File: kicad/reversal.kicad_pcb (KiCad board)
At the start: 2 copper layers, 256.2 x 134.5 mm, 27 parts, among them J1 USB_A

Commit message: reduced left edge of pcb
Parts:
- moved H4 19.9 mm to (256.0, 153.0)
- moved H3 15.3 mm to (29.0, 153.0)
- moved H5 4.84 mm to (29.0, 42.7)
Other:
- board size 256.2 x 134.5 mm -> 251.2 x 134.5 mm
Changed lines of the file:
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@@
   (net 27 "unconnected-(A1-3V3-Pad21)")
   (footprint "MountingHole:MountingHole_6.4mm_M6" (layer "F.Cu")
-    (at 24.16 42.7)
+    (at 29 42.7)
     (descr "Mounting Hole 6.4mm, no annular, M6")
     (tags "mounting hole 6.4mm no annular m6")
@@
   )
   (footprint "MountingHole:MountingHole_6.4mm_M6" (layer "F.Cu")
-    (at 236.3 150.1)
+    (at 256 153)
     (descr "Mounting Hole 6.4mm, no annular, M6")
     (tags "mounting hole 6.4mm no annular m6")
@@
   )
   (footprint "MountingHole:MountingHole_6.4mm_M6" (layer "F.Cu")
-    (at 44.06 150.13)
+    (at 29 153)
     (descr "Mounting Hole 6.4mm, no annular, M6")
     (tags "mounting hole 6.4mm no annular m6")
@@
   (gr_line (start 143.818526 116.498091) (end 143.365009 116.890938)
     (stroke (width 0.176388) (type solid)) (layer "Dwgs.User"))
-  (gr_arc (start 12.085449 40.725) (mid 15.000961 33.66137) (end 22.049924 30.710574)
+  (gr_arc (start 17.084488 40.725) (mid 20 33.66137) (end 27.048963 30.710574)
     (stroke (width 0.1) (type default)) (layer "Edge.Cuts"))
   (gr_line (start 258.150077 30.785573) (end 152.15 30.675)
@@
   (gr_line (start 152.15 52.175) (end 138.175 52.15)
     (stroke (width 0.1) (type default)) (layer "Edge.Cuts"))
-  (gr_line (start 138.175 30.675) (end 22.049924 30.710574)
+  (gr_line (start 138.175 30.675) (end 27.048963 30.710574)
     (stroke (width 0.1) (type default)) (layer "Edge.Cuts"))
-  (gr_arc (start 21.974923 165.114427) (mid 14.92596 162.163631) (end 12.010448 155.100001)
+  (gr_arc (start 26.973962 165.114427) (mid 19.924999 162.163631) (end 17.009487 155.100001)
     (stroke (width 0.1) (type default)) (layer "Edge.Cuts"))
-  (gr_line (start 12.085449 40.725) (end 12.010448 155.100001)
+  (gr_line (start 17.084488 40.725) (end 17.009487 155.100001)
     (stroke (width 0.1) (type default)) (layer "Edge.Cuts"))
-  (gr_line (start 21.974923 165.114427) (end 258.250077 165.164427)
+  (gr_line (start 26.973962 165.114427) (end 258.250077 165.164427)
     (stroke (width 0.1) (type default)) (layer "Edge.Cuts"))
   (gr_text "circle" (at 111.6 84.4) (layer "B.SilkS")

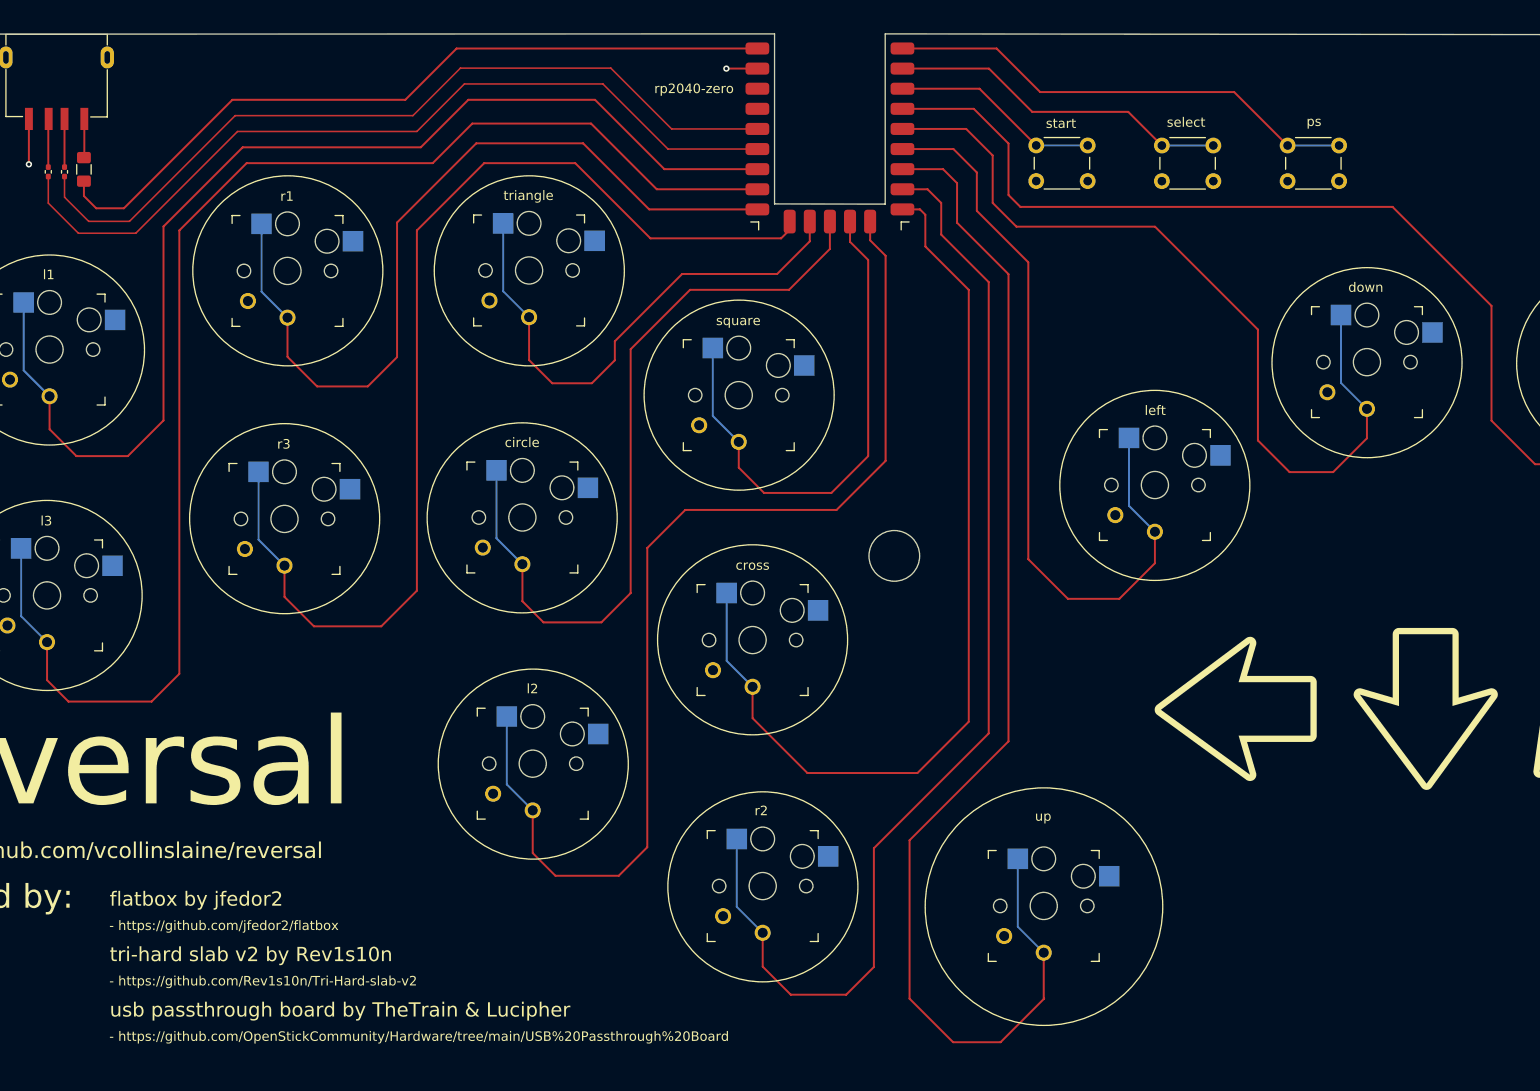
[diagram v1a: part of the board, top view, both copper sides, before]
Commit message: Added touch button & rerouted traces to accomodate
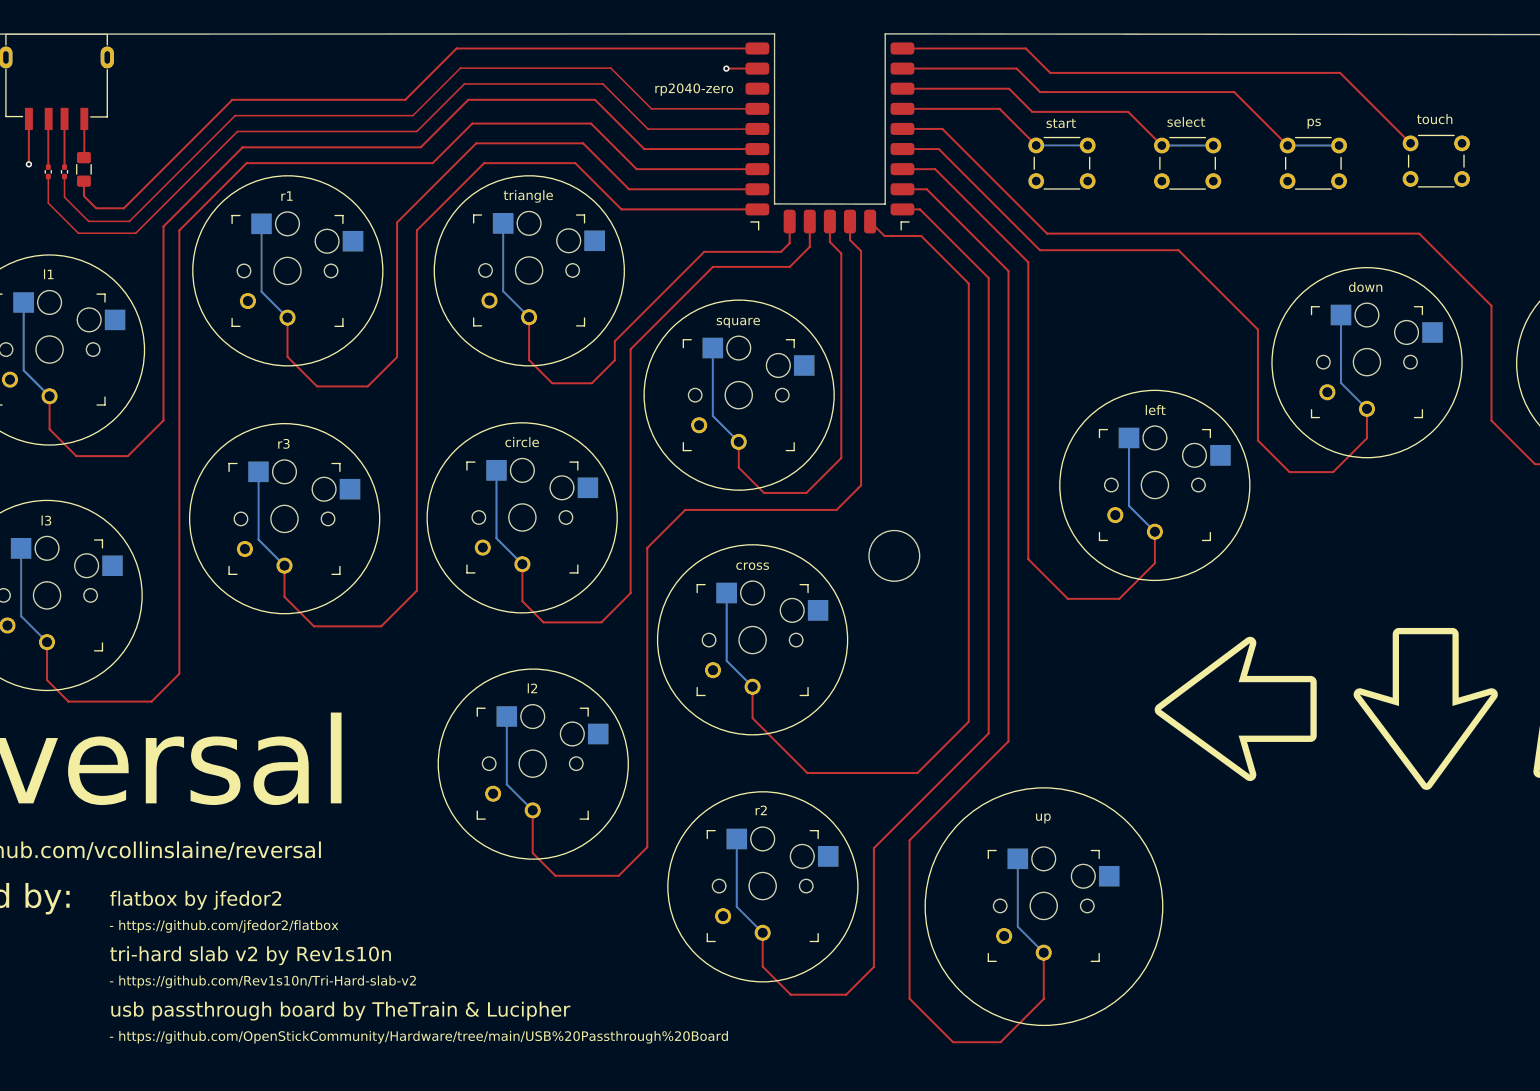
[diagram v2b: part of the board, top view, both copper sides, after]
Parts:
- added touch: SW_Push, Button_Switch_THT:SW_PUSH_6mm, F.Cu at (218.5, 44.5)
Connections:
- A1 pad 1: ps -> touch
- A1 pad 10: l2 -> cross
- A1 pad 11: square -> l2
- A1 pad 12: circle -> square
- A1 pad 13: triangle -> circle
- A1 pad 14: r3 -> triangle
- A1 pad 15: r1 -> r3
- A1 pad 16: l3 -> r1
- A1 pad 17: l1 -> l3
- A1 pad 18: D+ -> l1
- A1 pad 19: D- -> D+
- A1 pad 2: select -> ps
- A1 pad 20: unconnected-(A1-GPIO29-Pad20) -> D-
- A1 pad 3: start -> select
- A1 pad 4: right -> start
- A1 pad 5: down -> right
- A1 pad 6: left -> down
- A1 pad 7: up -> left
- A1 pad 8: r2 -> up
- A1 pad 9: cross -> r2
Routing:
- net touch: track 0.00 -> 69.1 mm
- net r3: track 138.8 -> 131.7 mm
- net right: track 138.5 -> 133.6 mm
- net down: track 107.0 -> 102.5 mm
- net left: track 99.3 -> 95.4 mm
- net up: track 159.1 -> 155.3 mm
- net square: track 66.6 -> 63.0 mm
- net r2: track 145.0 -> 141.9 mm
- net circle: track 98.9 -> 96.2 mm
- net triangle: track 66.6 -> 64.2 mm
- net cross: track 119.5 -> 121.1 mm
- net l2: track 139.2 -> 137.7 mm
- net start: track 26.4 -> 25.3 mm
- net select: track 43.3 -> 42.2 mm
- net r1: track 105.2 -> 104.1 mm
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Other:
- board text added: "touch"

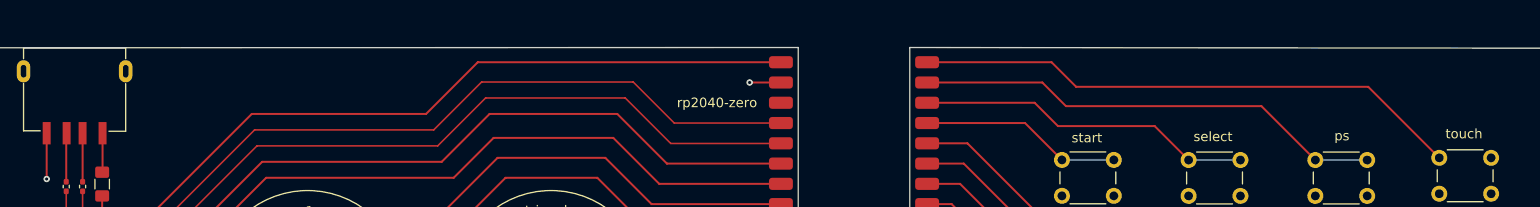
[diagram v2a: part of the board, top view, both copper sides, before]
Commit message: Fixed library linking issues
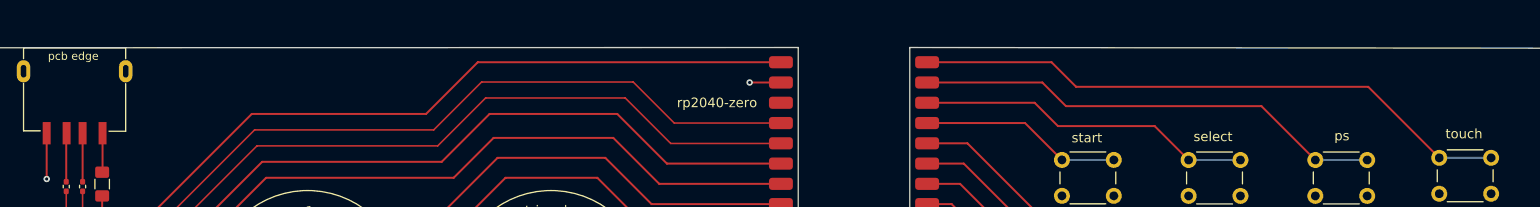
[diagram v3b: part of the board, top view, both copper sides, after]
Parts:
- J1: footprint Southpaw:USB_A_Female_C42425 -> Reversal:USB_A_Female_C42425
- renumbered touch to touch1
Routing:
- net touch: track 69.1 -> 75.6 mm
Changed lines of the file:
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@@
     (property "ki_keywords" "switch normally-open pushbutton push-button")
     (attr through_hole)
-    (fp_text reference "touch" (at 3.25 -2) (layer "F.SilkS") hide
+    (fp_text reference "touch1" (at 3.25 -2) (layer "F.SilkS") hide
         (effects (font (size 1 1) (thickness 0.15)))
     )
@@
       (net 2 "GND") (pinfunction "2") (pintype "passive"))
   )
-  (footprint "Southpaw:USB_A_Female_C42425" (layer "F.Cu")
+  (footprint "Reversal:USB_A_Female_C42425" (layer "F.Cu")
     (at 47.5 37.532 -90)
     (property "Sheetfile" "reversal.kicad_sch")
@@
         (effects (font (size 1 1) (thickness 0.1)))
     )
-    (fp_text value "USB_A" (at 0 11.05 -90 unlocked) (layer "F.Fab") hide
+    (fp_text value "USB_A" (at 0 11.05 -90 unlocked) (layer "F.Fab")
+        (effects (font (size 1 1) (thickness 0.15)))
+    )
+    (fp_text user "pcb edge" (at -5.19 3.35 unlocked) (layer "F.SilkS")
+        (effects (font (size 1 1) (thickness 0.1)) (justify left bottom))
+    )
+    (fp_text user "${REFERENCE}" (at 0 8.93 -90 unlocked) (layer "F.Fab")
         (effects (font (size 1 1) (thickness 0.15)))
     )
@@
   (segment (start 169.92 32.52) (end 173 35.6) (width 0.25) (layer "F.Cu") (net 26))
   (segment (start 173 35.6) (end 209.6 35.6) (width 0.25) (layer "F.Cu") (net 26))
+  (segment (start 218.5 44.5) (end 225 44.5) (width 0.25) (layer "B.Cu") (net 26))
   (zone (net 2) (net_name "GND") (layer "B.Cu") (hatch edge 0.5)
     (connect_pads (clearance 0.5))

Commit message: trace beautification
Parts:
- moved H1 1.71 mm to (153.1, 94.9)
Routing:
- net l2: track 137.7 -> 136.1 mm
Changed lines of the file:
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@@
         (effects (font (size 1 1) (thickness 0.15)))
     )
-    (fp_text user "pcb edge" (at -5.19 3.35 unlocked) (layer "F.SilkS")
-        (effects (font (size 1 1) (thickness 0.1)) (justify left bottom))
-    )
     (fp_text user "${REFERENCE}" (at 0 8.93 -90 unlocked) (layer "F.Fab")
         (effects (font (size 1 1) (thickness 0.15)))
@@
   )
   (footprint "MountingHole:MountingHole_6.4mm_M6" (layer "F.Cu")
-    (at 153.3 96.6)
+    (at 153.1 94.9)
     (descr "Mounting Hole 6.4mm, no annular, M6")
     (tags "mounting hole 6.4mm no annular m6")
@@
   (via (at 132.085 35.06) (size 0.8) (drill 0.4) (layers "F.Cu" "B.Cu") (net 2))
   (via (at 44 47.15) (size 0.8) (drill 0.4) (layers "F.Cu" "B.Cu") (net 2))
-  (segment (start 156.7 56.2) (end 152.065 56.2) (width 0.25) (layer "F.Cu") (net 3))
   (segment (start 156.221626 124.023064) (end 162.7 117.54469) (width 0.25) (layer "F.Cu") (net 3))
-  (segment (start 135.401626 117.101626) (end 142.323064 124.023064) (width 0.25) (layer "F.Cu") (net 3))
-  (segment (start 135.401626 113.133064) (end 135.401626 117.101626) (width 0.25) (layer "F.Cu") (net 3))
-  (segment (start 162.7 62.2) (end 156.7 56.2) (width 0.25) (layer "F.Cu") (net 3))
   (segment (start 162.7 117.54469) (end 162.7 62.2) (width 0.25) (layer "F.Cu") (net 3))
-  (segment (start 142.323064 124.023064) (end 156.221626 124.023064) (width 0.25) (layer "F.Cu") (net 3))
+  (segment (start 141.623064 124.023064) (end 156.221626 124.023064) (width 0.25) (layer "F.Cu") (net 3))
+  (segment (start 135.401626 113.133064) (end 135.401626 117.801626) (width 0.25) (layer "F.Cu") (net 3))
+  (segment (start 162.7 62.2) (end 156.7 56.2) (width 0.25) (layer "F.Cu") (net 3))
+  (segment (start 156.7 56.2) (end 152.065 56.2) (width 0.25) (layer "F.Cu") (net 3))
   (segment (start 152.065 56.2) (end 150.245 54.38) (width 0.25) (layer "F.Cu") (net 3))
+  (segment (start 135.401626 117.801626) (end 141.623064 124.023064) (width 0.25) (layer "F.Cu") (net 3))
   (segment (start 132.126626 109.858064) (end 135.401626 113.133064) (width 0.25) (layer "B.Cu") (net 3))
   (segment (start 132.126626 101.283064) (end 132.126626 109.858064) (width 0.25) (layer "B.Cu") (net 3))
@@
   (segment (start 136.005 32.52) (end 98.02 32.52) (width 0.25) (layer "F.Cu") (net 5))
   (segment (start 91.54 39) (end 69.7 39) (width 0.25) (layer "F.Cu") (net 5))
-  (segment (start 117.5 35) (end 98.5 35) (width 0.2) (layer "F.Cu") (net 6))
   (segment (start 92.5 41) (end 70.05 41) (width 0.2) (layer "F.Cu") (net 6))
+  (segment (start 98.6 34.9) (end 92.5 41) (width 0.2) (layer "F.Cu") (net 6))
   (segment (start 56.7 54.35) (end 51.55 54.35) (width 0.2) (layer "F.Cu") (net 6))
-  (segment (start 98.5 35) (end 92.5 41) (width 0.2) (layer "F.Cu") (net 6))
-  (segment (start 48.5 51.3) (end 48.5 48.695) (width 0.2) (layer "F.Cu") (net 6))
+  (segment (start 122.64 40.14) (end 117.4 34.9) (width 0.2) (layer "F.Cu") (net 6))
   (segment (start 70.05 41) (end 56.7 54.35) (width 0.2) (layer "F.Cu") (net 6))
   (segment (start 51.55 54.35) (end 48.5 51.3) (width 0.2) (layer "F.Cu") (net 6))
-  (segment (start 122.64 40.14) (end 136.005 40.14) (width 0.2) (layer "F.Cu") (net 6))
-  (segment (start 117.5 35) (end 122.64 40.14) (width 0.2) (layer "F.Cu") (net 6))
+  (segment (start 117.4 34.9) (end 98.6 34.9) (width 0.2) (layer "F.Cu") (net 6))
+  (segment (start 136.005 40.14) (end 122.64 40.14) (width 0.2) (layer "F.Cu") (net 6))
+  (segment (start 48.5 51.3) (end 48.5 48.695) (width 0.2) (layer "F.Cu") (net 6))
+  (segment (start 136.005 42.68) (end 135.985 42.7) (width 0.2) (layer "F.Cu") (net 7))
+  (segment (start 98.8 37.2) (end 93 43) (width 0.2) (layer "F.Cu") (net 7))
   (segment (start 46.45 52.05) (end 46.45 48.695) (width 0.2) (layer "F.Cu") (net 7))
+  (segment (start 122.2 42.7) (end 116.7 37.2) (width 0.2) (layer "F.Cu") (net 7))
+  (segment (start 70.35 43) (end 57.5 55.85) (width 0.2) (layer "F.Cu") (net 7))
   (segment (start 50.25 55.85) (end 46.45 52.05) (width 0.2) (layer "F.Cu") (net 7))
-  (segment (start 122.2 42.7) (end 116.5 37) (width 0.2) (layer "F.Cu") (net 7))
-  (segment (start 116.5 37) (end 99 37) (width 0.2) (layer "F.Cu") (net 7))
-  (segment (start 57.5 55.85) (end 50.25 55.85) (width 0.2) (layer "F.Cu") (net 7))
+  (segment (start 116.7 37.2) (end 98.8 37.2) (width 0.2) (layer "F.Cu") (net 7))
   (segment (start 93 43) (end 70.35 43) (width 0.2) (layer "F.Cu") (net 7))
-  (segment (start 136.005 42.68) (end 135.985 42.7) (width 0.2) (layer "F.Cu") (net 7))
-  (segment (start 99 37) (end 93 43) (width 0.2) (layer "F.Cu") (net 7))
-  (segment (start 70.35 43) (end 57.5 55.85) (width 0.2) (layer "F.Cu") (net 7))
+  (segment (start 57.5 55.85) (end 50.25 55.85) (width 0.2) (layer "F.Cu") (net 7))
   (segment (start 135.985 42.7) (end 122.2 42.7) (width 0.2) (layer "F.Cu") (net 7))
+  (segment (start 98.9 39.6) (end 93.5 45) (width 0.25) (layer "F.Cu") (net 9))
+  (segment (start 121.72 45.22) (end 116.1 39.6) (width 0.25) (layer "F.Cu") (net 9))
   (segment (start 61 55) (end 61 79.5) (width 0.25) (layer "F.Cu") (net 9))
-  (segment (start 50 84) (end 46.611626 80.611626) (width 0.25) (layer "F.Cu") (net 9))
-  (segment (start 115.5 39) (end 99.5 39) (width 0.25) (layer "F.Cu") (net 9))
+  (segment (start 93.5 45) (end 71 45) (width 0.25) (layer "F.Cu") (net 9))
   (segment (start 46.611626 80.611626) (end 46.611626 76.443064) (width 0.25) (layer "F.Cu") (net 9))
-  (segment (start 99.5 39) (end 93.5 45) (width 0.25) (layer "F.Cu") (net 9))
-  (segment (start 121.72 45.22) (end 115.5 39) (width 0.25) (layer "F.Cu") (net 9))
   (segment (start 61 79.5) (end 56.5 84) (width 0.25) (layer "F.Cu") (net 9))
-  (segment (start 93.5 45) (end 71 45) (width 0.25) (layer "F.Cu") (net 9))
-  (segment (start 136.005 45.22) (end 121.72 45.22) (width 0.25) (layer "F.Cu") (net 9))
   (segment (start 56.5 84) (end 50 84) (width 0.25) (layer "F.Cu") (net 9))
+  (segment (start 50 84) (end 46.611626 80.611626) (width 0.25) (layer "F.Cu") (net 9))
+  (segment (start 116.1 39.6) (end 98.9 39.6) (width 0.25) (layer "F.Cu") (net 9))
   (segment (start 71 45) (end 61 55) (width 0.25) (layer "F.Cu") (net 9))
+  (segment (start 136.005 45.22) (end 121.72 45.22) (width 0.25) (layer "F.Cu") (net 9))
   (segment (start 43.336626 73.168064) (end 46.611626 76.443064) (width 0.25) (layer "B.Cu") (net 9))
   (segment (start 43.336626 64.593064) (end 43.336626 73.168064) (width 0.25) (layer "B.Cu") (net 9))
-  (segment (start 146 90.8) (end 126.9 90.8) (width 0.25) (layer "F.Cu") (net 10))
+  (segment (start 107.631626 134.131626) (end 107.631626 128.743064) (width 0.25) (layer "F.Cu") (net 10))
+  (segment (start 149.1 84.9) (end 143.2 90.8) (width 0.25) (layer "F.Cu") (net 10))
+  (segment (start 143.2 90.8) (end 126.9 90.8) (width 0.25) (layer "F.Cu") (net 10))
   (segment (start 110.5 137) (end 107.631626 134.131626) (width 0.25) (layer "F.Cu") (net 10))
-  (segment (start 122.1 95.6) (end 122.1 133.4) (width 0.25) (layer "F.Cu") (net 10))
+  (segment (start 126.9 90.8) (end 122.1 95.6) (width 0.25) (layer "F.Cu") (net 10))
   (segment (start 118.5 137) (end 110.5 137) (width 0.25) (layer "F.Cu") (net 10))
-  (segment (start 149.1 87.7) (end 148.7 88.1) (width 0.25) (layer "F.Cu") (net 10))
   (segment (start 122.1 133.4) (end 118.5 137) (width 0.25) (layer "F.Cu") (net 10))
-  (segment (start 147.705 56.705) (end 149.1 58.1) (width 0.25) (layer "F.Cu") (net 10))
-  (segment (start 107.631626 134.131626) (end 107.631626 128.743064) (width 0.25) (layer "F.Cu") (net 10))
+  (segment (start 149.1 58.1) (end 149.1 84.9) (width 0.25) (layer "F.Cu") (net 10))
+  (segment (start 122.1 95.6) (end 122.1 133.4) (width 0.25) (layer "F.Cu") (net 10))
   (segment (start 147.705 54.38) (end 147.705 56.705) (width 0.25) (layer "F.Cu") (net 10))
-  (segment (start 148.7 88.1) (end 146 90.8) (width 0.25) (layer "F.Cu") (net 10))
-  (segment (start 149.1 58.1) (end 149.1 87.7) (width 0.25) (layer "F.Cu") (net 10))
-  (segment (start 126.9 90.8) (end 122.1 95.6) (width 0.25) (layer "F.Cu") (net 10))
+  (segment (start 147.705 56.705) (end 149.1 58.1) (width 0.25) (layer "F.Cu") (net 10))
   (segment (start 104.356626 116.893064) (end 104.356626 125.468064) (width 0.25) (layer "B.Cu") (net 10))
   (segment (start 104.356626 125.468064) (end 107.631626 128.743064) (width 0.25) (layer "B.Cu") (net 10))

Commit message: Matched differential pair to usb2 spec
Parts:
- H1, H2, H3, H4, H5: footprint MountingHole:MountingHole_6.4mm_M6 -> MountingHole:MountingHole_5.3mm_M5
- moved R4 3.10 mm to (46.5, 45.0)
- moved R5 3.10 mm to (48.5, 45.0)
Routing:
- net D-: track 101.6 -> 105.2 mm
- net Net-(J1-D-): track 6.09 -> 2.98 mm
- net Net-(J1-D+): track 6.11 -> 3.01 mm
- net D+: track 104.5 -> 106.5 mm
